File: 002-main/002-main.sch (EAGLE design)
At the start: 46 parts, among them IC1 MEGA8-MI, J1 22057045, J2 22057045, J3 22057035, J4 22057035, J5 22057035, J6 22057035, J7 22057035, U2 STM32F446RET6, X1 Seeed Studio XIAO ESP32C3

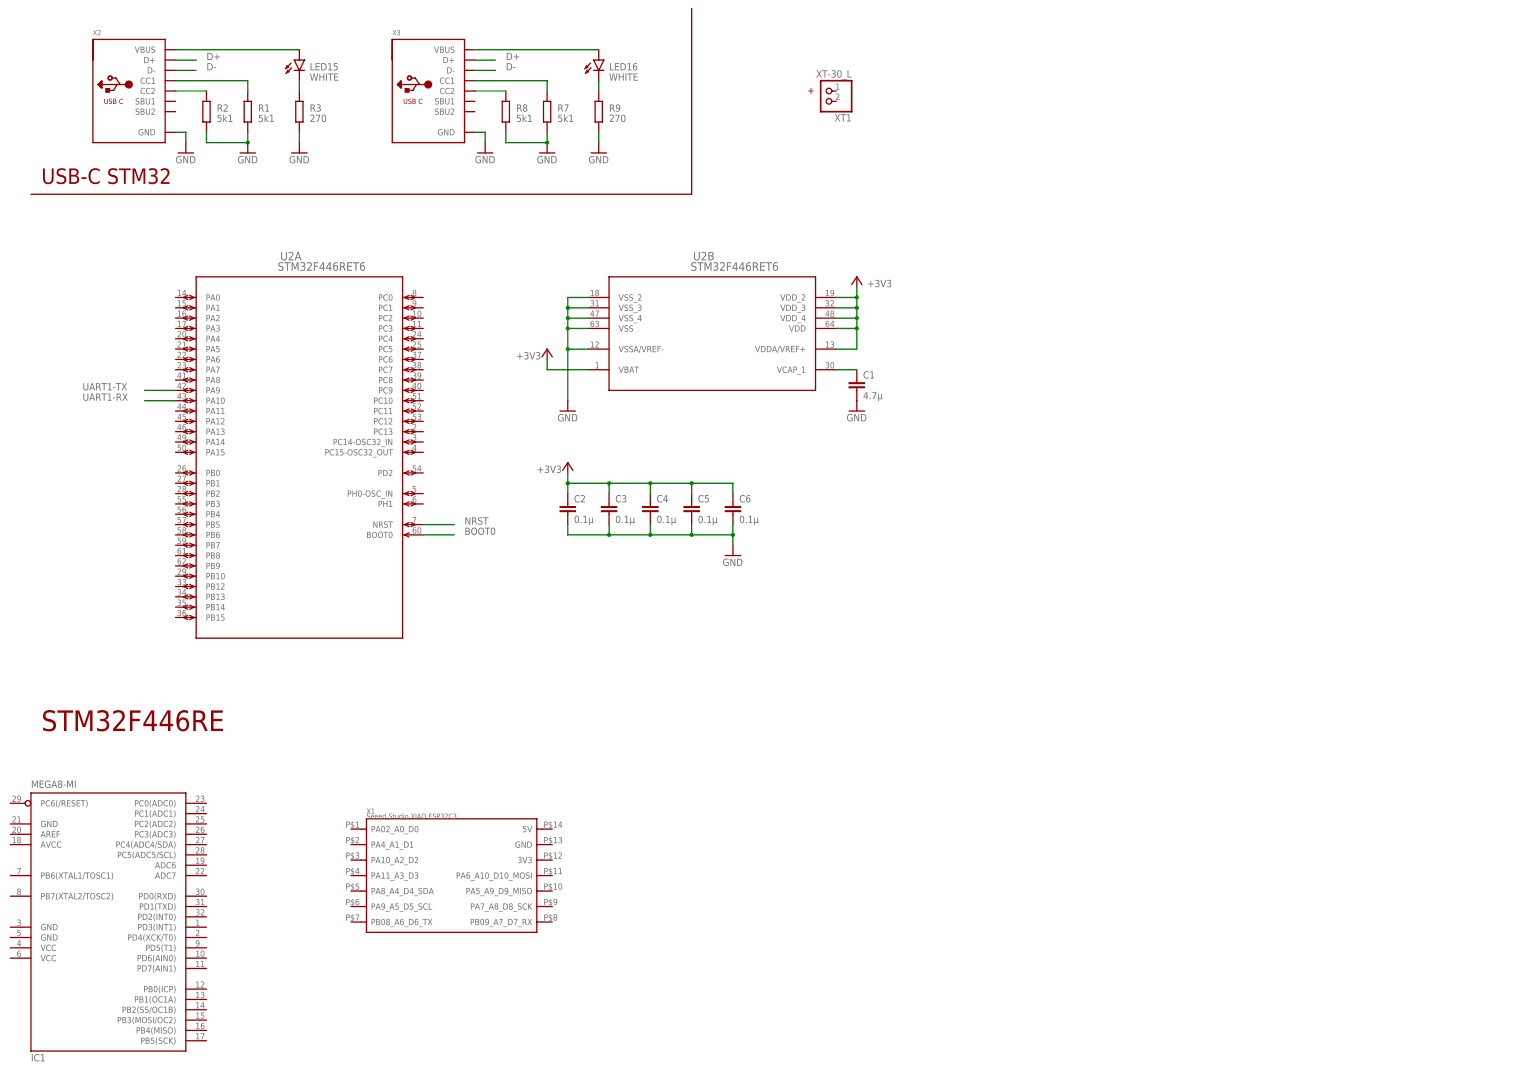
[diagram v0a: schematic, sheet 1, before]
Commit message: ジャイロ配置
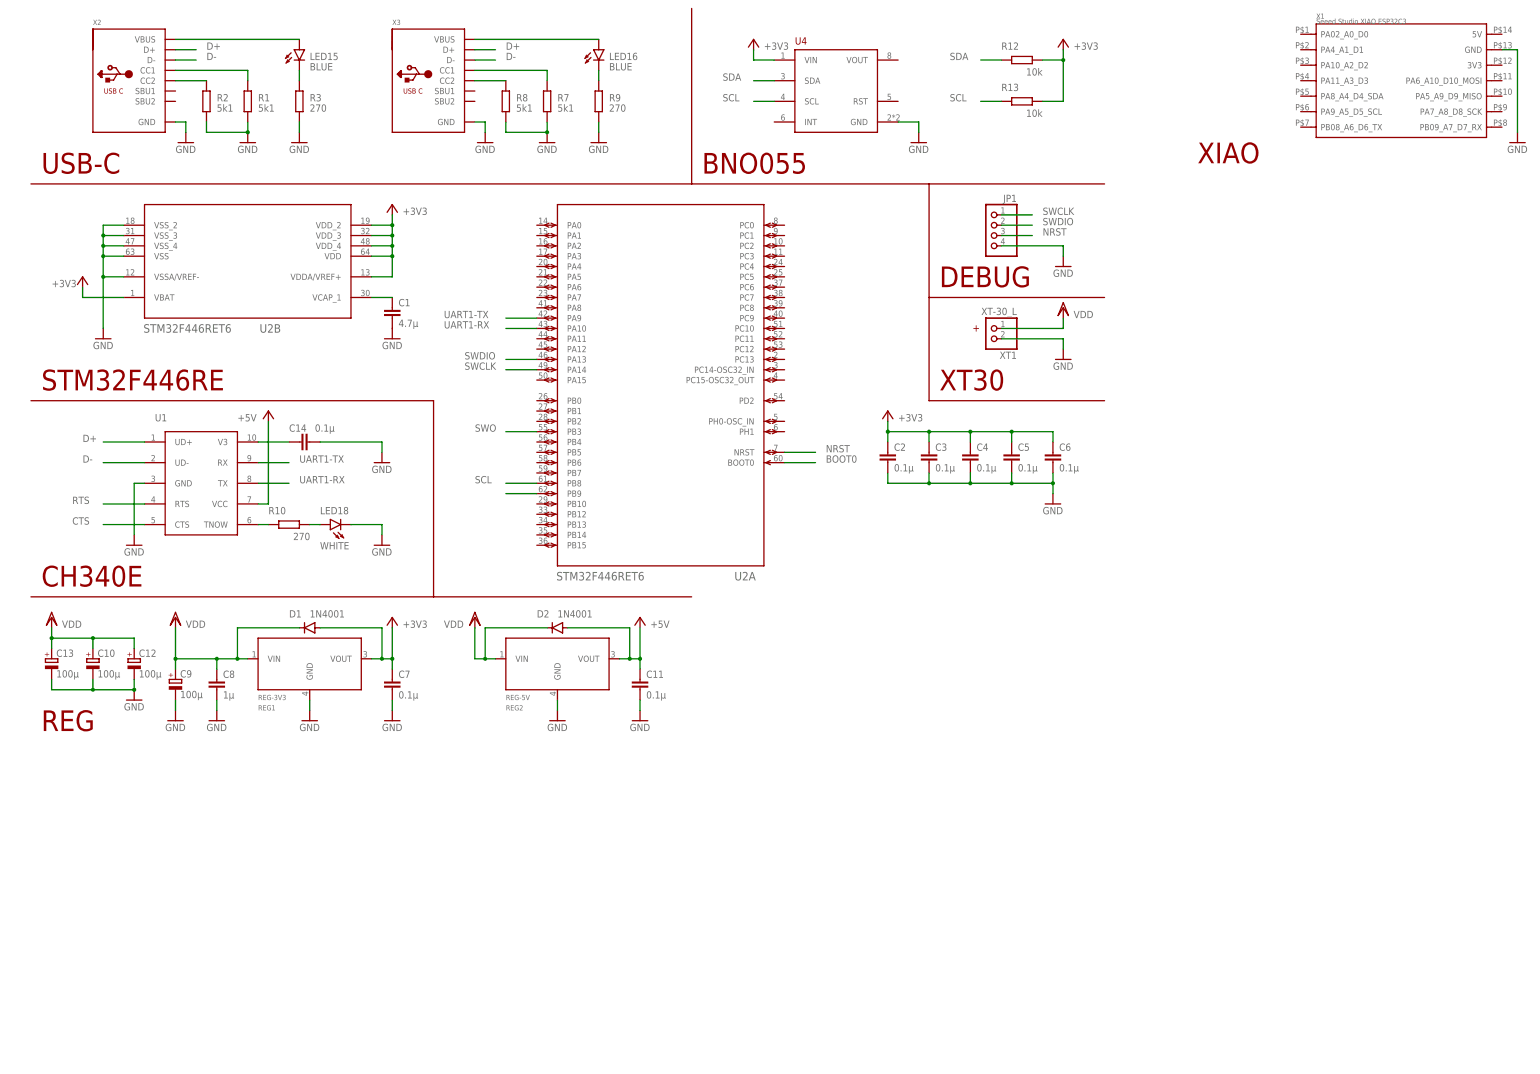
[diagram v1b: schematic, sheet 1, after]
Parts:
- added C10, C12, C13, C9: 100μ, rcl:CPOL-EU153CLV-0505
- added C11, C14, C15, C7: 0.1µ, rcl:C-EUC0603
- added C8: 1µ, rcl:C-EUC0603
- added D1, D2: 1N4001, diode:GF1
- added J8: 5267-5, con-molex-spox:5267-5
- added JP1: (no value), pinhead:PINHD-1X4/90
- added LED18, LED19: WHITE, led:LEDSML0603
- added R10, R11: 270, rcl:R-EU_R0402
- added R12, R13: 10k, rcl:R-EU_R0402
- added REG1: REG-3V3, #001-line:MYPARTS_NJM7800S-REGULATOR
- added REG2: REG-5V, #001-line:MYPARTS_NJM7800S-REGULATOR
- added U1, U3: CH340ESMD, CH340E:CH340ESMD
- added U4: (no value), BNO055:BNO055
- added Y1: 16MHz, 7325-0800A2010-00:O3225100MEDA4SC
- IC1: value MEGA8-MI -> MEGA8-AI; device atmel:MEGA8-MI -> atmel:MEGA8-AI
- LED15, LED16: value WHITE -> BLUE
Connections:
- net LED_SIDE_5V renamed LED-L
- new net AVR-CTS: U3.CTS
- new net AVR-RTS: U3.RTS
- new net AVR-RX: IC1.PD0(RXD), U3.TX
- new net AVR-TX: IC1.PD1(TXD), U3.RX
- new net CTS: U1.CTS
- new net LED-R: LED8.DI
- new net N$22: R10.2, U1.TNOW
- new net N$23: LED18.A, R10.1
- new net N$24: C15.1, U3.V3
- new net N$25: R11.2, U3.TNOW
- new net N$26: LED19.A, R11.1
- new net OSC1: IC1.PB6(XTAL1/TOSC1), Y1.E/D
- new net OSC2: IC1.PB7(XTAL2/TOSC2), Y1.OUTPUT
- new net RTS: U1.RTS
- new net SCL: R13.2, U2A.PB8, U4.SCL
- new net SDA: R12.2, U2A.PB9, U4.SDA
- new net SERVO-SIG: J3.1, J4.1, J5.1, J6.1, J7.1
- new net SWCLK: JP1.1, U2A.PA14
- new net SWDIO: JP1.2, U2A.PA13
- new net SWO: U2A.PB3
- new net TOP-LED: J8.-5
- new net TOP-RX: J8.-4
- new net TOP-TX: J8.-3
- new net VDD: C10.+, C12.+, C13.+, C8.1, C9.+, D1.C, D2.C, J3.3, J4.3, J5.3, J6.3, J7.3, J8.-1, REG1.VIN, REG2.VIN, XT1.1
- net +3V3: now also C7.1, D1.A, R12.1, R13.1, REG1.VOUT, U4.VIN
- net +5V: now also C11.1, D2.A, IC1.VCC@1, IC1.VCC@2, REG2.VOUT, U1.VCC, U3.VCC
- net AVR-D+: now also U3.UD+
- net AVR-D-: now also U3.UD-
- net D+: now also U1.UD+
- net D-: now also U1.UD-
- net GND: now also C10.-, C11.2, C12.-, C13.-, C14.2, C15.2, C7.2, C8.2, C9.-, IC1.GND, IC1.GND@1, IC1.GND@2, J3.2, J4.2, J5.2, J6.2, J7.2, J8.-2, JP1.4, LED18.C, LED19.C, REG1.GND, REG2.GND, U1.GND, U3.GND, U4.GND, X1.GND, XT1.2, Y1.GND, Y1.VDD
- net N$8: now also C14.1, U1.V3; no longer LED7.DO, LED8.DI
- net NRST: now also JP1.3
- net UART1-RX: now also U1.TX
- net UART1-TX: now also U1.RX
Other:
- note added: "BNO055"
- note added: "CH340E"
- note added: "CONN-CAM"
- note added: "CONN-SERVO"
- note added: "CONN-TOP"
- note added: "DEBUG"
- note added: "REG"
- note added: "USB-C"
- note added: "XIAO"
- note added: "XT30"
- note removed: "USB-C STM32"
- moved on the sheet: C1, C2, C3, C4, C5, C6, J1, J2, J3, J4, J5, J6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

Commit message: UART配線完了
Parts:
- added J9: 5267-4, con-molex-spox:5267-4
- added Q1: C1015, transistor-pnp:BCX71SMD
- added R14: 20k, rcl:R-EU_R0402
- added R15, R16: 5k1, rcl:R-EU_R0402
- added R17: 270, rcl:R-EU_R0402
- added U5: MAX485ESA+T, MAX485:MAX485ESA+T
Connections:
- removed net TOP-RX: J8.-4
- removed net TOP-TX: J8.-3
- new net !RE: Q1.C, R14.1, U5.!RE, U5.DE
- new net LED-UI: J9.-4
- new net N$27: Q1.B, R17.1
- new net N$28: R15.2, R16.1, U5.B
- new net SW1: J9.-3
- new net SW2: J9.-2
- new net TOGGLE: J9.-1
- new net UART2-RX: J2.4, U2A.PA3
- new net UART2-TX: J2.3, U2A.PA2
- new net UART3-RX: U2A.PC5, X1.PB08_A6_D6_TX
- new net UART3-TX: U2A.PB10, X1.PB09_A7_D7_RX
- new net UART4-RX: J8.-4, U2A.PA1
- new net UART4-TX: J8.-3, U2A.PA0
- new net UART5-RX: U2A.PD2, U5.RO
- new net UART5-TX: R17.2, U2A.PC12, U5.DI
- new net UART6-RX: J1.4, U2A.PC7
- new net UART6-TX: J1.3, U2A.PC6
- net +5V: now also J1.2, J2.2, Q1.E, R15.1, U5.VCC
- net GND: now also J1.1, J2.1, R14.2, R16.2, U5.GND
- net SERVO-SIG: now also U5.A
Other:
- note added: "CAM"
- note added: "RS485"
- note added: "TOP"
- note removed: "CONN-CAM"
- note removed: "CONN-TOP"
- moved on the sheet: C14, C15, C2, C3, C4, C5, C6, J1, J2, J8, LED17, LED18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
